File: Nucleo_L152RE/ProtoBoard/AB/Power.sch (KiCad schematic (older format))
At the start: 26 parts, among them J1 EXTPower, P10 ServoPower, P11 Power1, P7 Power2, P8 Power3, P9 VinPower, U1 LDS3985

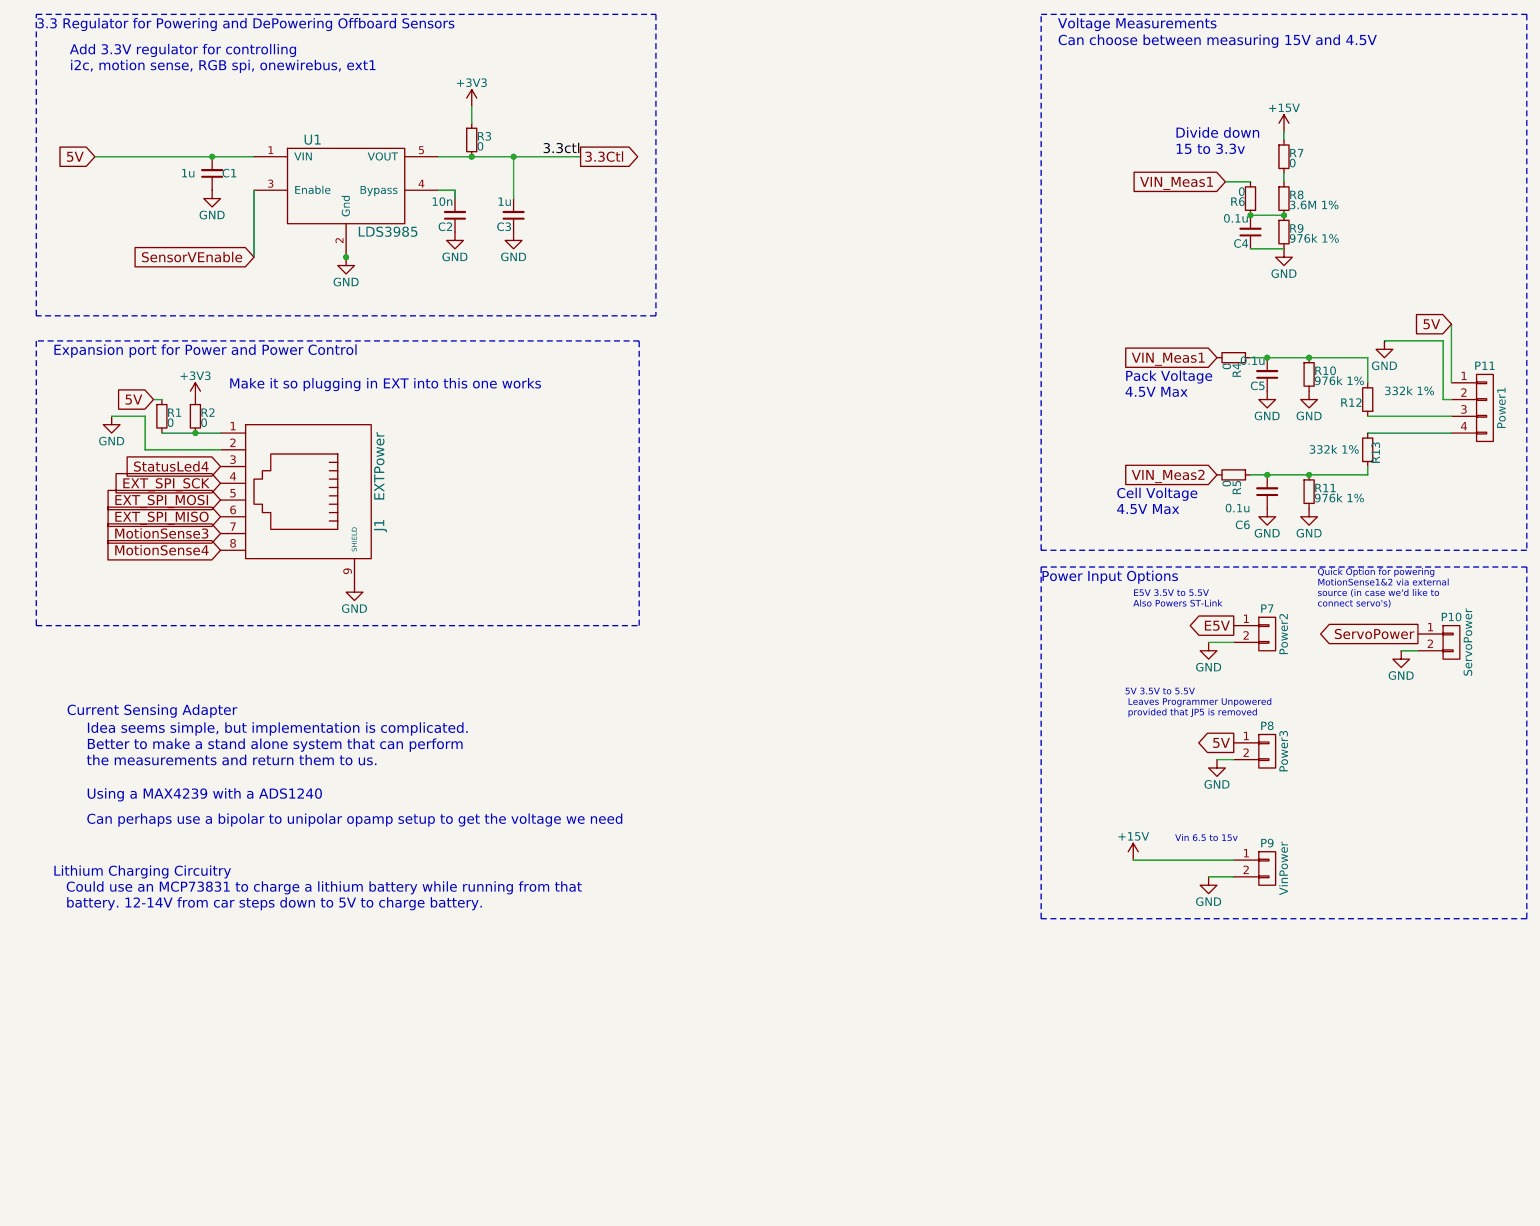
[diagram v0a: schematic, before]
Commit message: Components mostly laid out into final resting positions with exception of plethora of single pin connections for easily connecting to GND, 3.3V, 5V, 3.3Vctl.
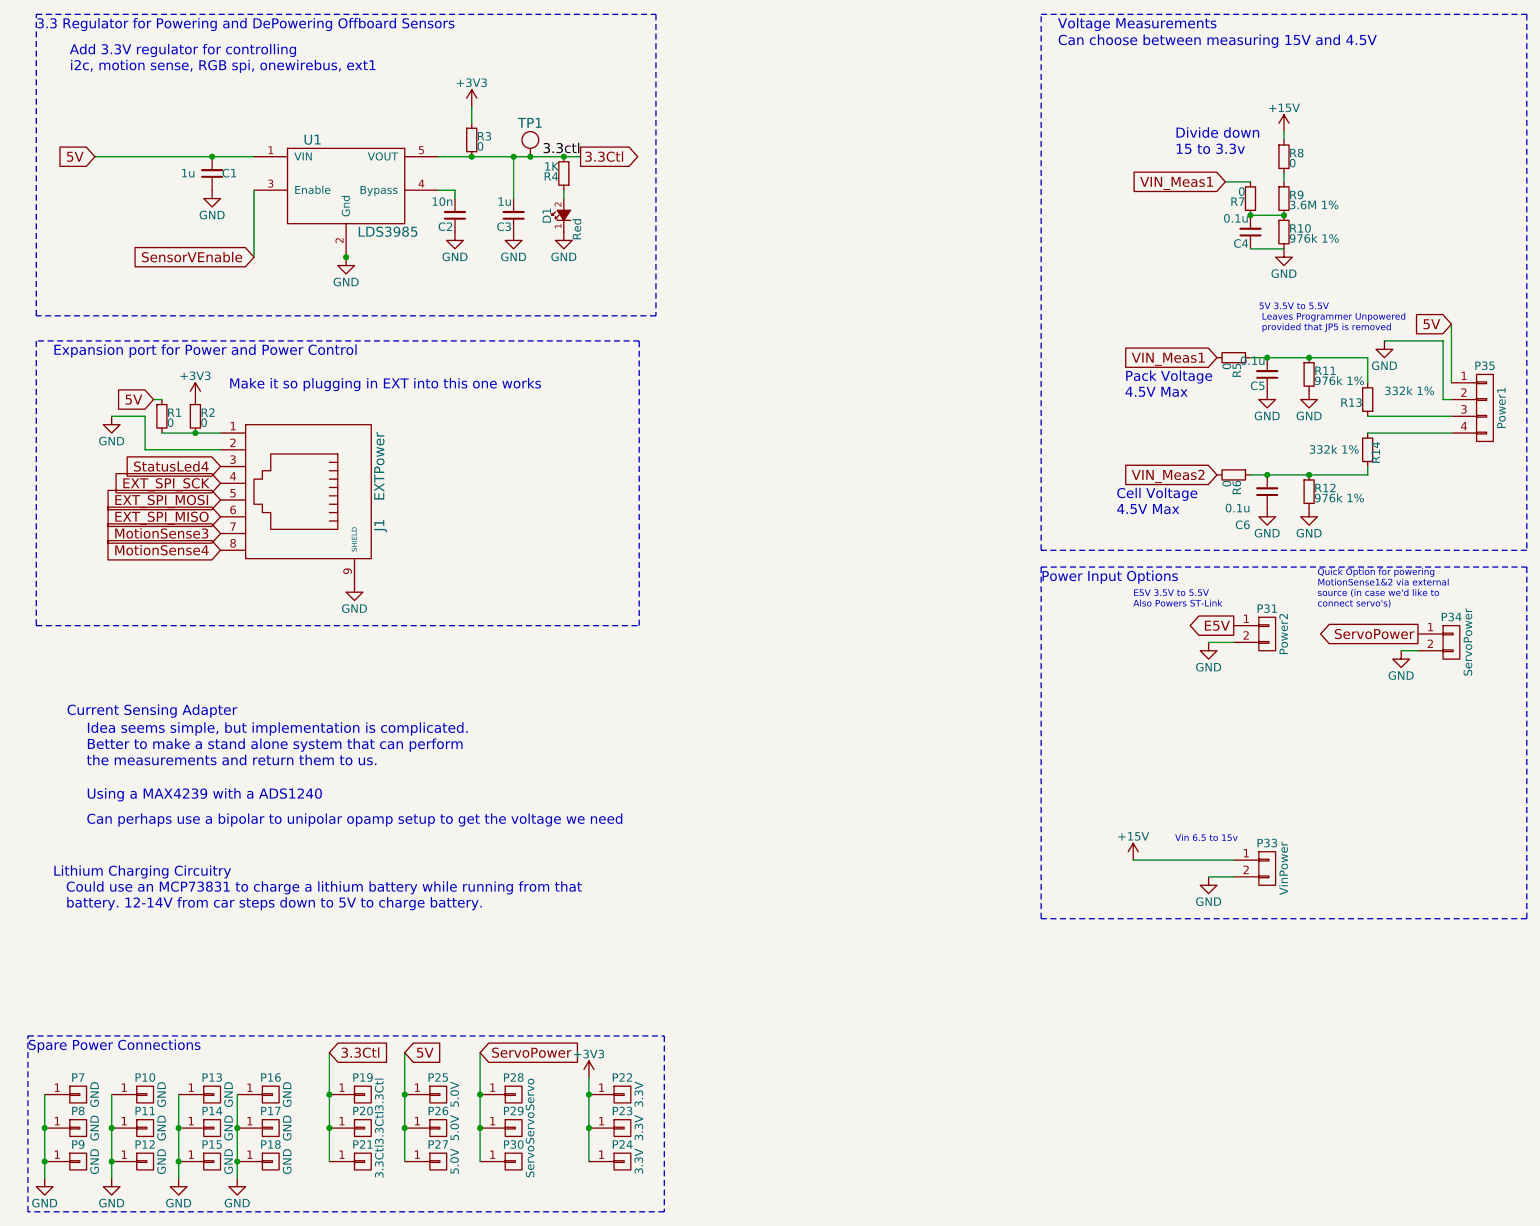
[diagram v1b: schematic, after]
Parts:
- removed P8: Power3, Pin_Headers:Pin_Header_Straight_1x02, symbol CONN_01X02
- added D1: Red, nucleo:LED_0603_Standard, symbol Led_Small
- added P10, P11, P12, P13, P14, P15, P16, P17, P18, P7, P8, P9: GND, Pin_Headers:Pin_Header_Straight_1x01, symbol CONN_01X01
- added P19, P20, P21: 3.3Ctl, Pin_Headers:Pin_Header_Straight_1x01, symbol CONN_01X01
- added P22, P23, P24: 3.3V, Pin_Headers:Pin_Header_Straight_1x01, symbol CONN_01X01
- added P25, P26, P27: 5.0V, Pin_Headers:Pin_Header_Straight_1x01, symbol CONN_01X01
- added P28, P29, P30: Servo, Pin_Headers:Pin_Header_Straight_1x01, symbol CONN_01X01
- added R4: 1K, Resistors_SMD:R_0603_HandSoldering, symbol R_Small
- added TP1: tp, nucleo:TestPoint_1mm, symbol tp
- renumbered P7 to P31, P9 to P33, P10 to P34, P11 to P35, R9 to R10, R10 to R11, R11 to R12, R12 to R13, R13 to R14, R4 to R5, R5 to R6, R6 to R7, R7 to R8, R8 to R9
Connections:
- net +3V3: now also P22.1 (P1), P23.1 (P1), P24.1 (P1)
- net 3.3Ctl: now also P19.1 (P1), P20.1 (P1), P21.1 (P1), R4.2, TP1.1
- net 5V: now also P25.1 (P1), P26.1 (P1), P27.1 (P1)
- net GND: now also D1.1 (K), P10.1 (P1), P11.1 (P1), P12.1 (P1), P13.1 (P1), P14.1 (P1), P15.1 (P1), P16.1 (P1), P17.1 (P1), P18.1 (P1), P7.1 (P1), P8.1 (P1), P9.1 (P1)
- net ServoPower: now also P28.1 (P1), P29.1 (P1), P30.1 (P1)
- new net: D1.2 (A), R4.1
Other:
- note added: "Spare Power Connections"
